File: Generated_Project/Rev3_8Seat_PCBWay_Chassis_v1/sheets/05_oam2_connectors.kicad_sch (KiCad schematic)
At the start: 0 parts

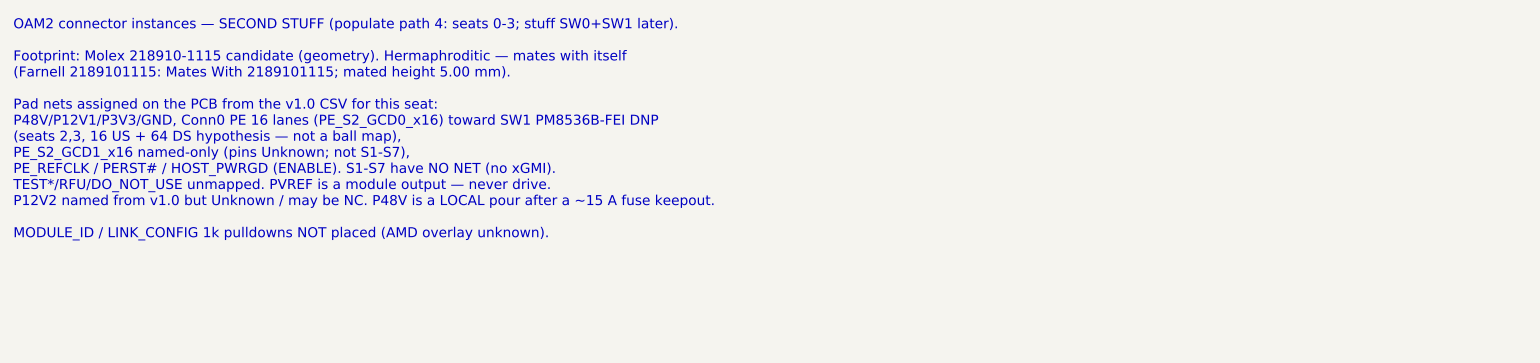
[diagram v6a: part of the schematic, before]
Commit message: Retarget Rev3 first article to seats 0-1 GCD0 x16 (2-module path).
Same 8-seat PCB. Without overlay, 2x MI250X means two modules can sit
and at most GCD0 on each can be named toward the host keepout (2 GCDs),
not 2x full-width (4 GCDs). Conn0 OCP PCIE_* is the only legal host PE.
No CEM/MCIO MPN. Do not energize P48V.

Co-authored-by: zivzancoeli-commits <zivzancoeli-commits@users.noreply.github.com>
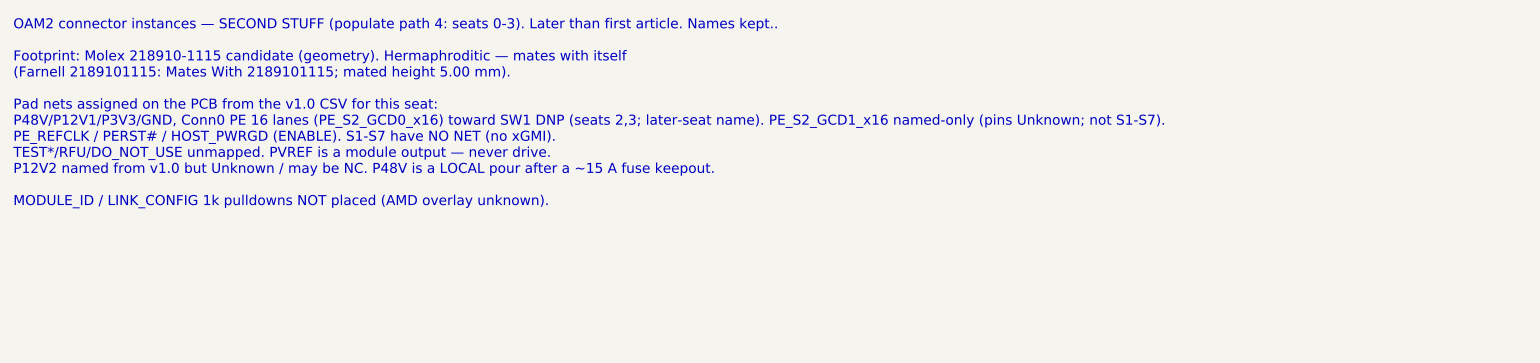
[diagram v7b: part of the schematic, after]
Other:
- note added: "OAM2 connector instances — SECOND STUFF (populate path 4: seats 0-3). Later than first article. Names kept.. Footprint: Molex 218910-1115 candidate (geometry). Hermaphroditic — mates with itself (Farnell 2189101115: Mates With 2189101115; mated height 5.00 mm). Pad nets assigned on the PCB from the v1.0 CSV for this seat: P48V/P12V1/P3V3/GND, Conn0 PE 16 lanes (PE_S2_GCD0_x16) toward SW1 DNP (sea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"
- note removed: "OAM2 connector instances — SECOND STUFF (populate path 4: seats 0-3; stuff SW0+SW1 later). Footprint: Molex 218910-1115 candidate (geometry). Hermaphroditic — mates with itself (Farnell 2189101115: Mates With 2189101115; mated height 5.00 mm). Pad nets assigned on the PCB from the v1.0 CSV for this seat: P48V/P12V1/P3V3/GND, Conn0 PE 16 lanes (PE_S2_GCD0_x16) toward SW1 PM8536B-FEI DNP (seats 2,3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"
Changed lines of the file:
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@@
         (comment 4 "r2.0 UNUSABLE. P3V3=Conn0 C1/C2. 12L 2.0mm stuffed-switch TARGET. 4x PM8536 DNP. Star-fed P48V.")
 	)
-	(text "OAM2 connector instances — SECOND STUFF (populate path 4: seats 0-3; stuff SW0+SW1 later).\n\nFootprint: Molex 218910-1115 candidate (geometry). Hermaphroditic — mates with itself\n(Farnell 2189101115: Mates With 2189101115; mated height 5.00 mm).\n\nPad nets assigned on the PCB from the v1.0 CSV for this seat:\nP48V/P12V1/P3V3/GND, Conn0 PE 16 lanes (PE_S2_GCD0_x16) toward SW1 PM8536B-FEI DNP\n(seats 2,3, 16 US + 64 DS hypothesis — not a ball map),\nPE_S2_GCD1_x16 named-only (pins Unknown; not S1-S7),\nPE_REFCLK / PERST# / HOST_PWRGD (ENABLE). S1-S7 have NO NET (no xGMI).\nTEST*/RFU/DO_NOT_USE unmapped. PVREF is a module output — never drive.\nP12V2 named from v1.0 but Unknown / may be NC. P48V is a LOCAL pour after a ~15 A fuse keepout.\n\nMODULE_ID / LINK_CONFIG 1k pulldowns NOT placed (AMD overlay unknown).\n"
+	(text "OAM2 connector instances — SECOND STUFF (populate path 4: seats 0-3). Later than first article. Names kept..\n\nFootprint: Molex 218910-1115 candidate (geometry). Hermaphroditic — mates with itself\n(Farnell 2189101115: Mates With 2189101115; mated height 5.00 mm).\n\nPad nets assigned on the PCB from the v1.0 CSV for this seat:\nP48V/P12V1/P3V3/GND, Conn0 PE 16 lanes (PE_S2_GCD0_x16) toward SW1 DNP (seats 2,3; later-seat name). PE_S2_GCD1_x16 named-only (pins Unknown; not S1-S7).\nPE_REFCLK / PERST# / HOST_PWRGD (ENABLE). S1-S7 have NO NET (no xGMI).\nTEST*/RFU/DO_NOT_USE unmapped. PVREF is a module output — never drive.\nP12V2 named from v1.0 but Unknown / may be NC. P48V is a LOCAL pour after a ~15 A fuse keepout.\n\nMODULE_ID / LINK_CONFIG 1k pulldowns NOT placed (AMD overlay unknown).\n"
 		(exclude_from_sim no)
 		(at 20.32 20.32 0)
